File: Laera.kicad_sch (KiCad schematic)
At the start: 38 parts, among them J1 USB_C_Receptacle_USB2.0_16P, J2 Conn_ST_STDC14, Q1 NMOS, Q2 NMOS, U2 E22-900M22S, U3 USBLC6-2P6, U4 BME680, U5 AMS1117-3.3, U6 STM32U083CCUx, Y1 24MHz

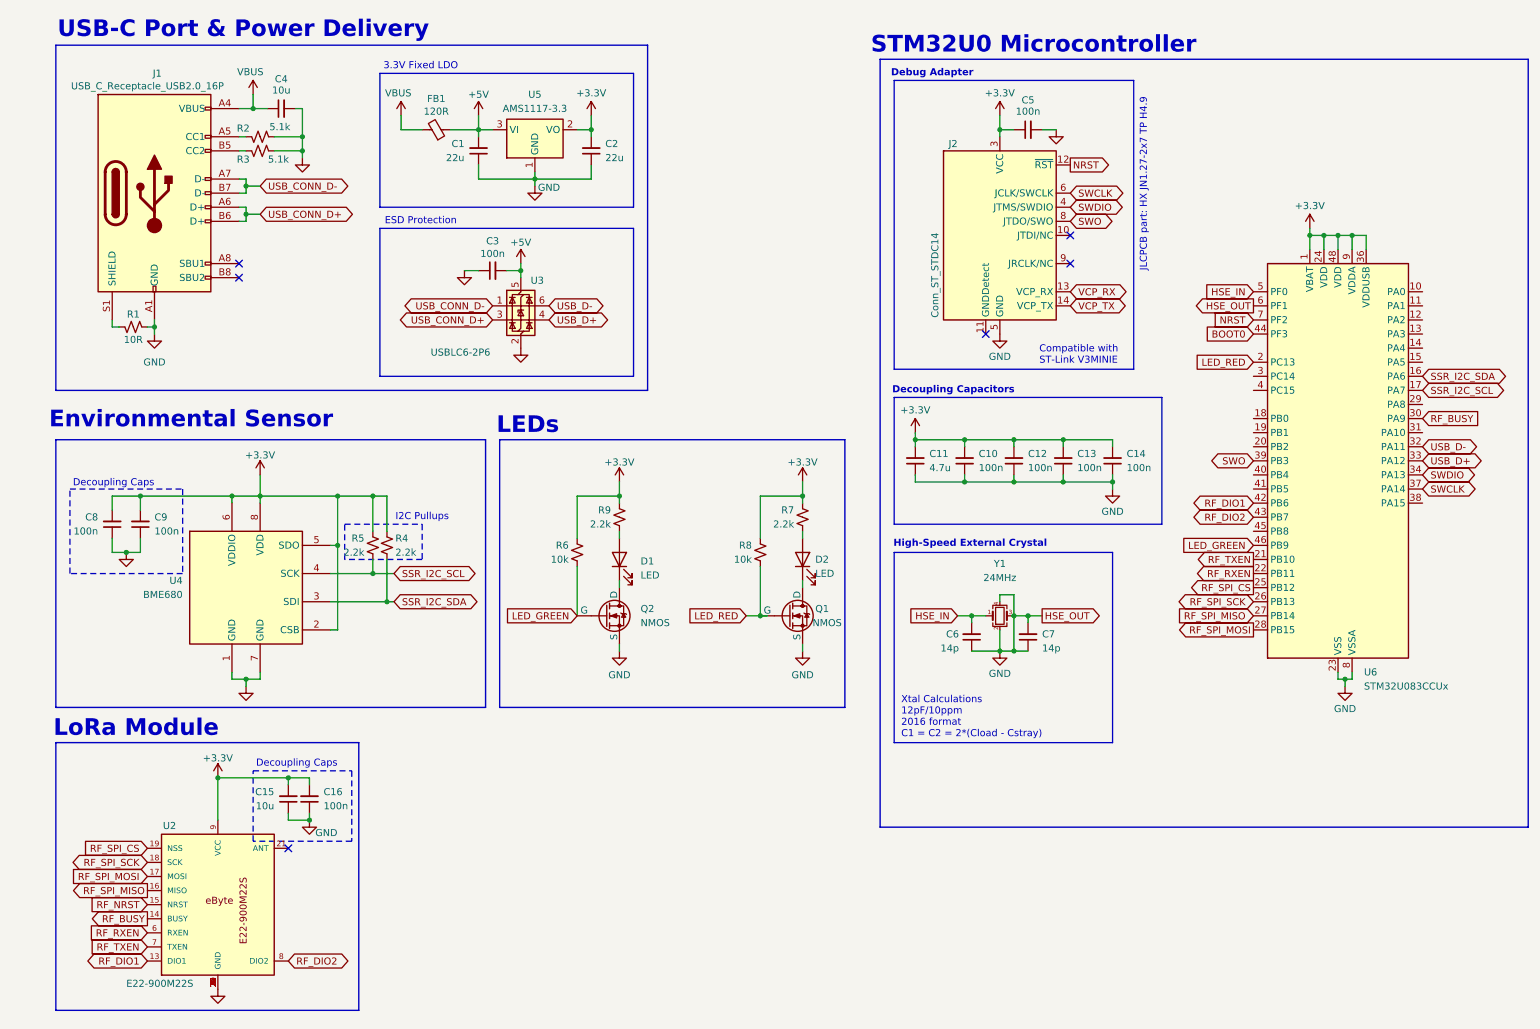
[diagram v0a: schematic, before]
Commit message: Finished ERC + Started Layout
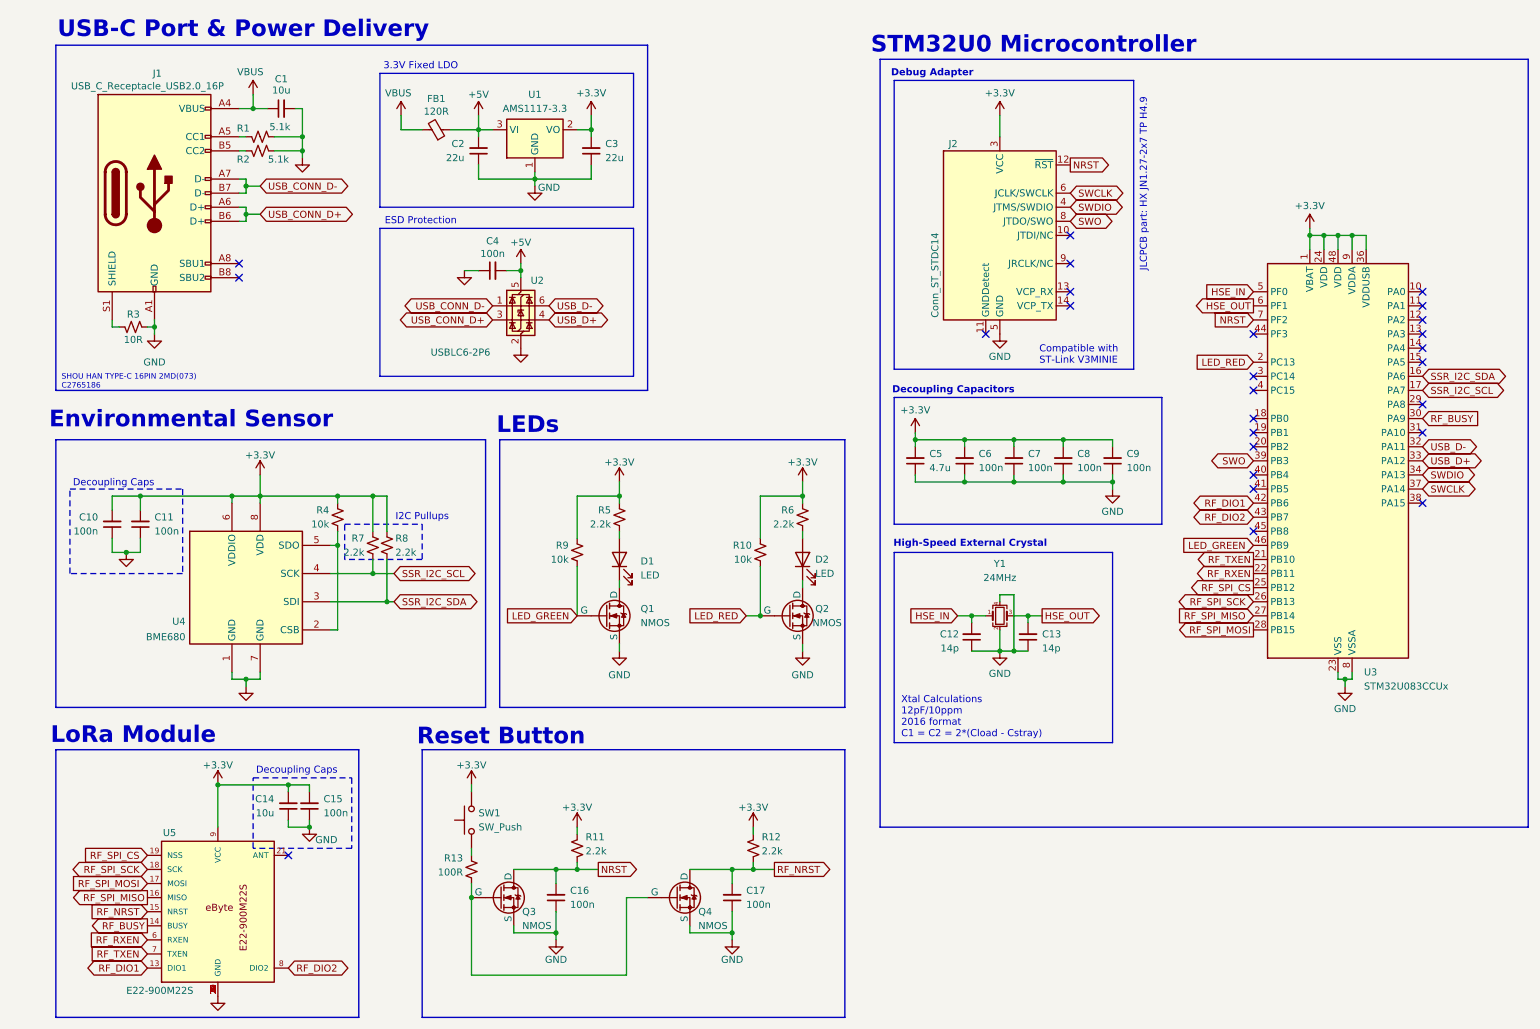
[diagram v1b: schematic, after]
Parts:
- removed C5: 100n, symbol Device:C_Small
- added C16, C17: 100n, Capacitor_SMD:C_0603_1608Metric, symbol Device:C_Small
- added Q3, Q4: NMOS, Package_TO_SOT_SMD:SOT-23, symbol Simulation_SPICE:NMOS
- added R11, R12: 2.2k, Resistor_SMD:R_0603_1608Metric, symbol Device:R_Small_US
- added R13: 100R, Resistor_SMD:R_0603_1608Metric, symbol Device:R_Small_US
- added R4: 10k, Resistor_SMD:R_0603_1608Metric, symbol Device:R_Small_US
- added SW1: SW_Push, Button_Switch_SMD:SW_Push_1P1T_NO_CK_KMR2, symbol Switch:SW_Push
- C1: renamed from C4; footprint (none) -> Capacitor_SMD:C_0603_1608Metric
- C10: renamed from C8; footprint (none) -> Capacitor_SMD:C_0603_1608Metric
- C11: renamed from C9; footprint (none) -> Capacitor_SMD:C_0603_1608Metric
- C12: renamed from C6; footprint (none) -> Capacitor_SMD:C_0603_1608Metric
- C13: renamed from C7; footprint (none) -> Capacitor_SMD:C_0603_1608Metric
- C14: renamed from C15; footprint (none) -> Capacitor_SMD:C_0603_1608Metric
- C15: renamed from C16; footprint (none) -> Capacitor_SMD:C_0603_1608Metric
- C2: renamed from C1; footprint (none) -> Capacitor_SMD:C_0603_1608Metric
- C3: renamed from C2; footprint (none) -> Capacitor_SMD:C_0603_1608Metric
- C4: renamed from C3; footprint (none) -> Capacitor_SMD:C_0603_1608Metric
- C5: renamed from C11; footprint (none) -> Capacitor_SMD:C_0603_1608Metric
- C6: renamed from C10; footprint (none) -> Capacitor_SMD:C_0603_1608Metric
- C7: renamed from C12; footprint (none) -> Capacitor_SMD:C_0603_1608Metric
- C8: renamed from C13; footprint (none) -> Capacitor_SMD:C_0603_1608Metric
- C9: renamed from C14; footprint (none) -> Capacitor_SMD:C_0603_1608Metric
- D1, D2: footprint (none) -> LED_SMD:LED_0603_1608Metric
- FB1: footprint (none) -> Inductor_SMD:L_0603_1608Metric
- J1: footprint (none) -> MyFootprints:CONN16_C16PIN_SHN
- Q1: renamed from Q2; footprint (none) -> Package_TO_SOT_SMD:SOT-23
- Q2: renamed from Q1; footprint (none) -> Package_TO_SOT_SMD:SOT-23
- R1: renamed from R2; footprint (none) -> Resistor_SMD:R_0603_1608Metric
- R10: renamed from R8; footprint (none) -> Resistor_SMD:R_0603_1608Metric
- R2: renamed from R3; footprint (none) -> Resistor_SMD:R_0603_1608Metric
- R3: renamed from R1; footprint (none) -> Resistor_SMD:R_0603_1608Metric
- R5: renamed from R9; footprint (none) -> Resistor_SMD:R_0603_1608Metric
- R6: renamed from R7; footprint (none) -> Resistor_SMD:R_0603_1608Metric
- R7: renamed from R5; footprint (none) -> Resistor_SMD:R_0603_1608Metric
- R8: renamed from R4; footprint (none) -> Resistor_SMD:R_0603_1608Metric
- R9: renamed from R6; footprint (none) -> Resistor_SMD:R_0603_1608Metric
- Y1: footprint (none) -> Crystal:Crystal_SMD_2016-4Pin_2.0x1.6mm
- renumbered U5 to U1, U3 to U2, U6 to U3, U2 to U5
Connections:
- net +3.3V: now also R11.2, R12.2, R4.2, SW1.2; no longer U4.2 (CSB), U4.5 (SDO)
- net GND: now also C16.1, C17.1, Q3.3 (S), Q4.3 (S); no longer C13.2, U3.6 (PF1), Y1.3
- net NRST: now also C16.2, Q3.1 (D), R11.1
- net RF_NRST: now also C17.2, Q4.1 (D), R12.1
- net BOOT0: no longer names the net of U3.44 (PF3)
- net VCP_RX: no longer names the net of J2.13 (VCP_RX)
- net VCP_TX: no longer names the net of J2.14 (VCP_TX)
- new net: R13.2, SW1.1
- new net: Q3.2 (G), Q4.2 (G), R13.1
- new net: R4.1, U4.2 (CSB), U4.5 (SDO)
- new net HSE_OUT: C13.2, U3.6 (PF1), Y1.3
- no-connect marks 6 -> 26
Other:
- note added: "Reset Button"
- note added: "SHOU HAN TYPE-C 16PIN 2MD(073) C2765186"
- moved on the sheet: C14, C15, U5
